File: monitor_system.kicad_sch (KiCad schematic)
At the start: 3 parts, among them K1 DIPxx-1Axx-11x, U1 ACS781xLRTR-050B, U2 L7805

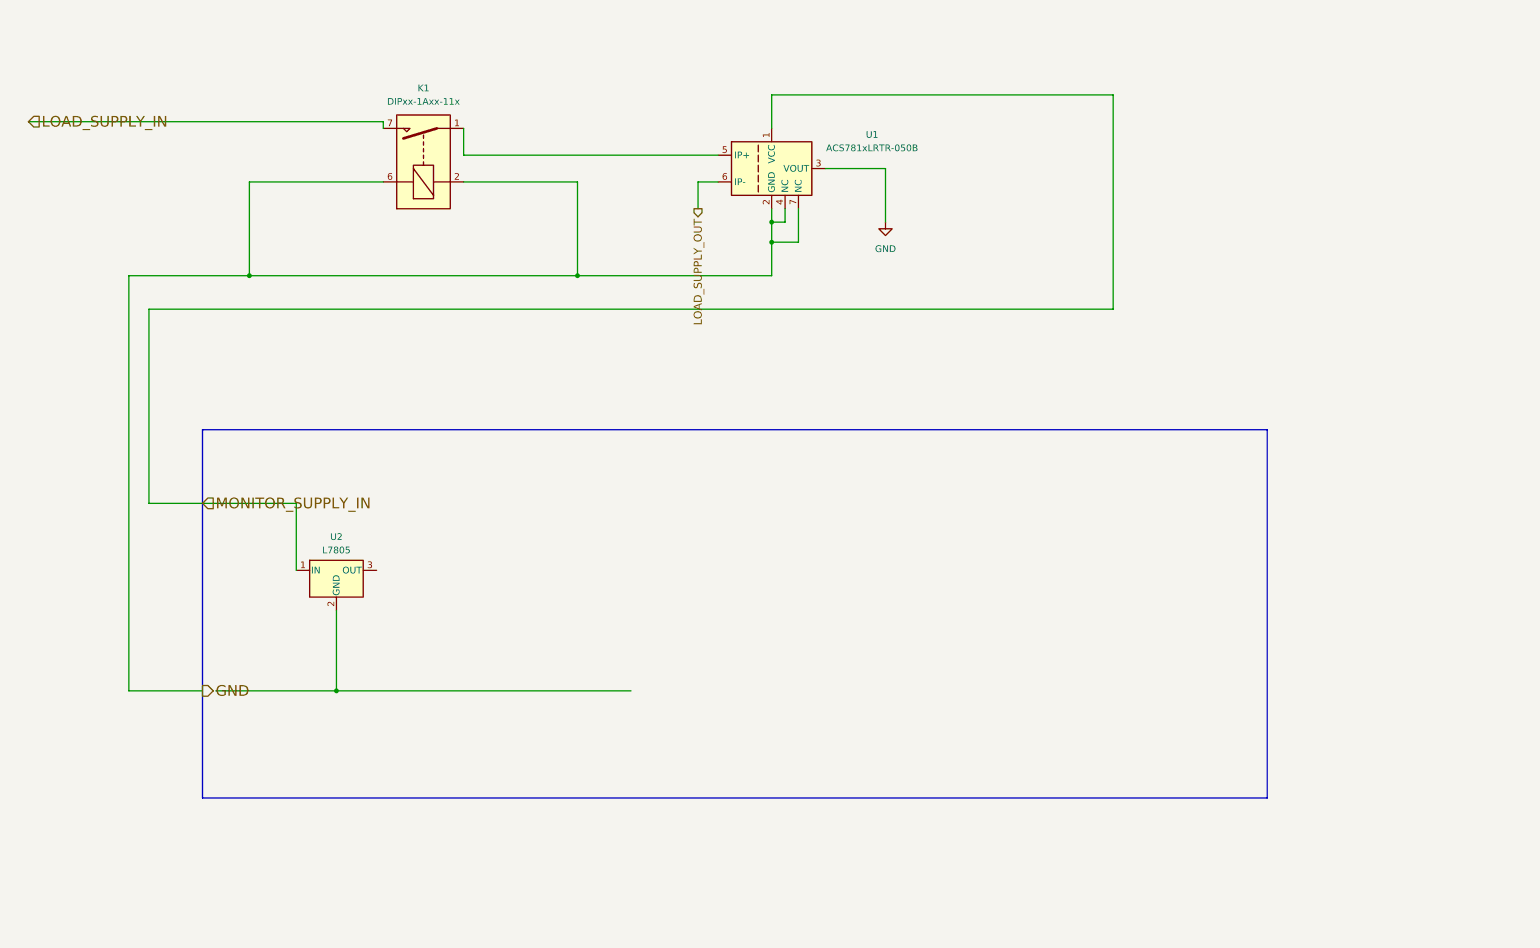
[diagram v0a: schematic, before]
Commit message: feat: new Circuit elements in the schematic and new LTspice Model
feat:added latch in kicad schematic with relative sheet

feat:added Analog-comparator in kicad schematic

feat:added LTspice Analog-comparator model

feat:added spice model into Models folder for the Analog_comparator

refactor:moved all LTspice simulation in a single folder for each one
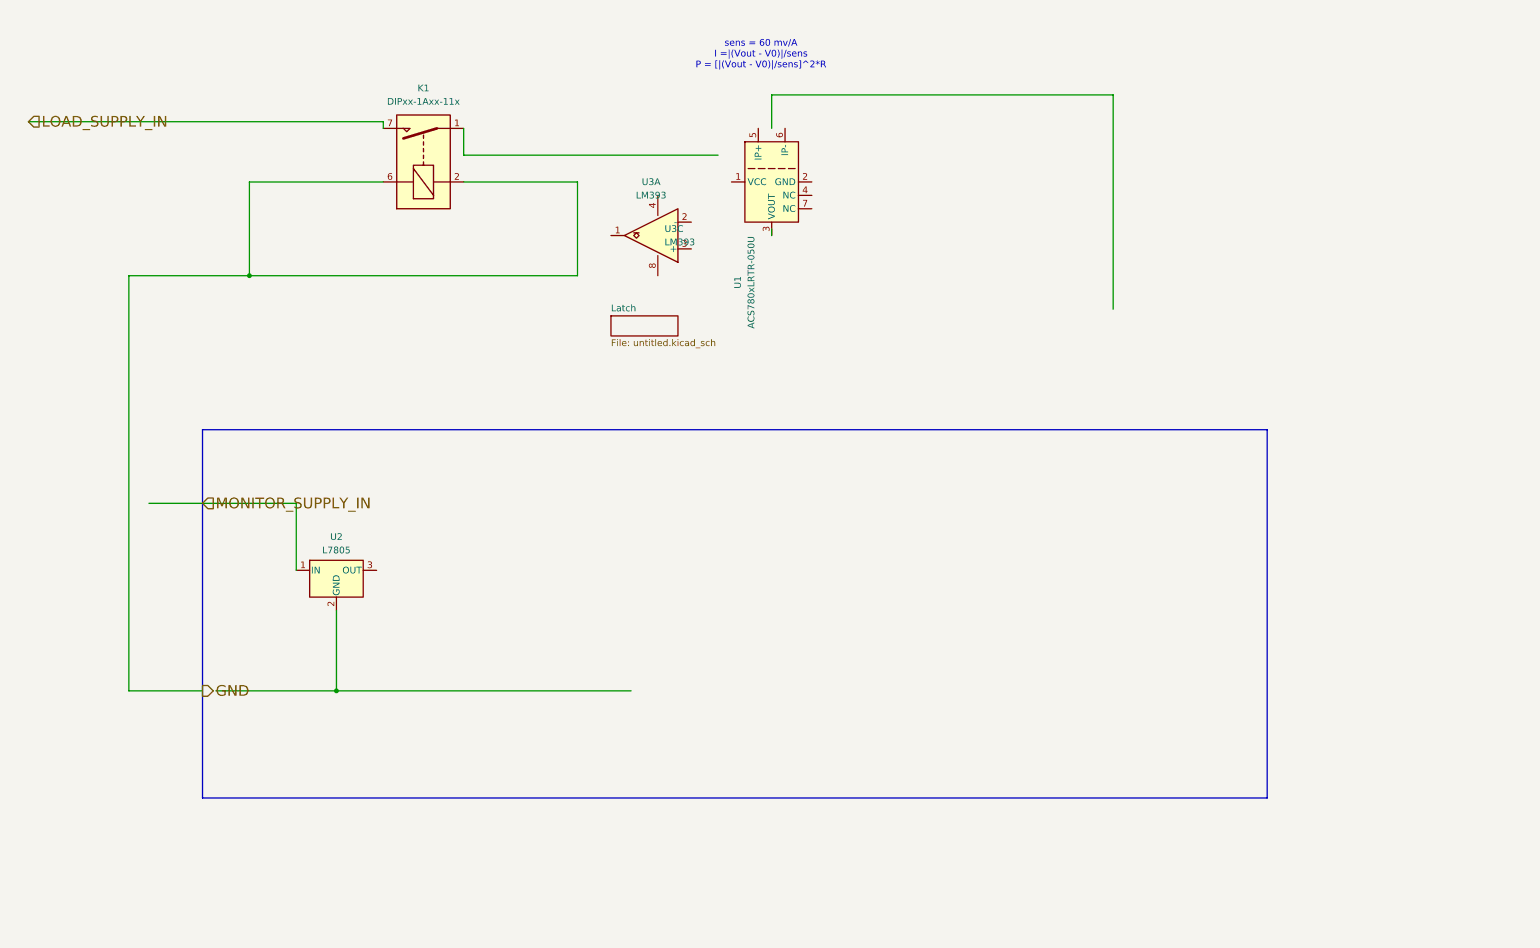
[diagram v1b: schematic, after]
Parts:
- removed U1: ACS781xLRTR-050B, Sensor_Current:Allegro_PSOF-7_4.8x6.4mm_P1.60mm, symbol Sensor_Current:ACS781xLRTR-050B
- added U1: ACS780xLRTR-050U, Sensor_Current:Allegro_PSOF-7_4.8x6.4mm_P1.60mm, symbol Sensor_Current:ACS780xLRTR-050U
- added U3: LM393, symbol Comparator:LM393
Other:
- added sheet Latch (untitled.kicad_sch)
- note added: "sens = 60 mv/A I =|(Vout - V0)|/sens P = [|(Vout - V0)|/sens]^2*R"

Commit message: feat + fix + refactor on the kicad schematic and simulation folder
feat:added transistor for coil supply

refractor: deleted latch sheet

feat: added latch connection

refractor: the monito logic and the supply are now separated

feat:added labels for connection

feat:added falstad NAND latch simulation

ERC = not tested
DRC = not tested
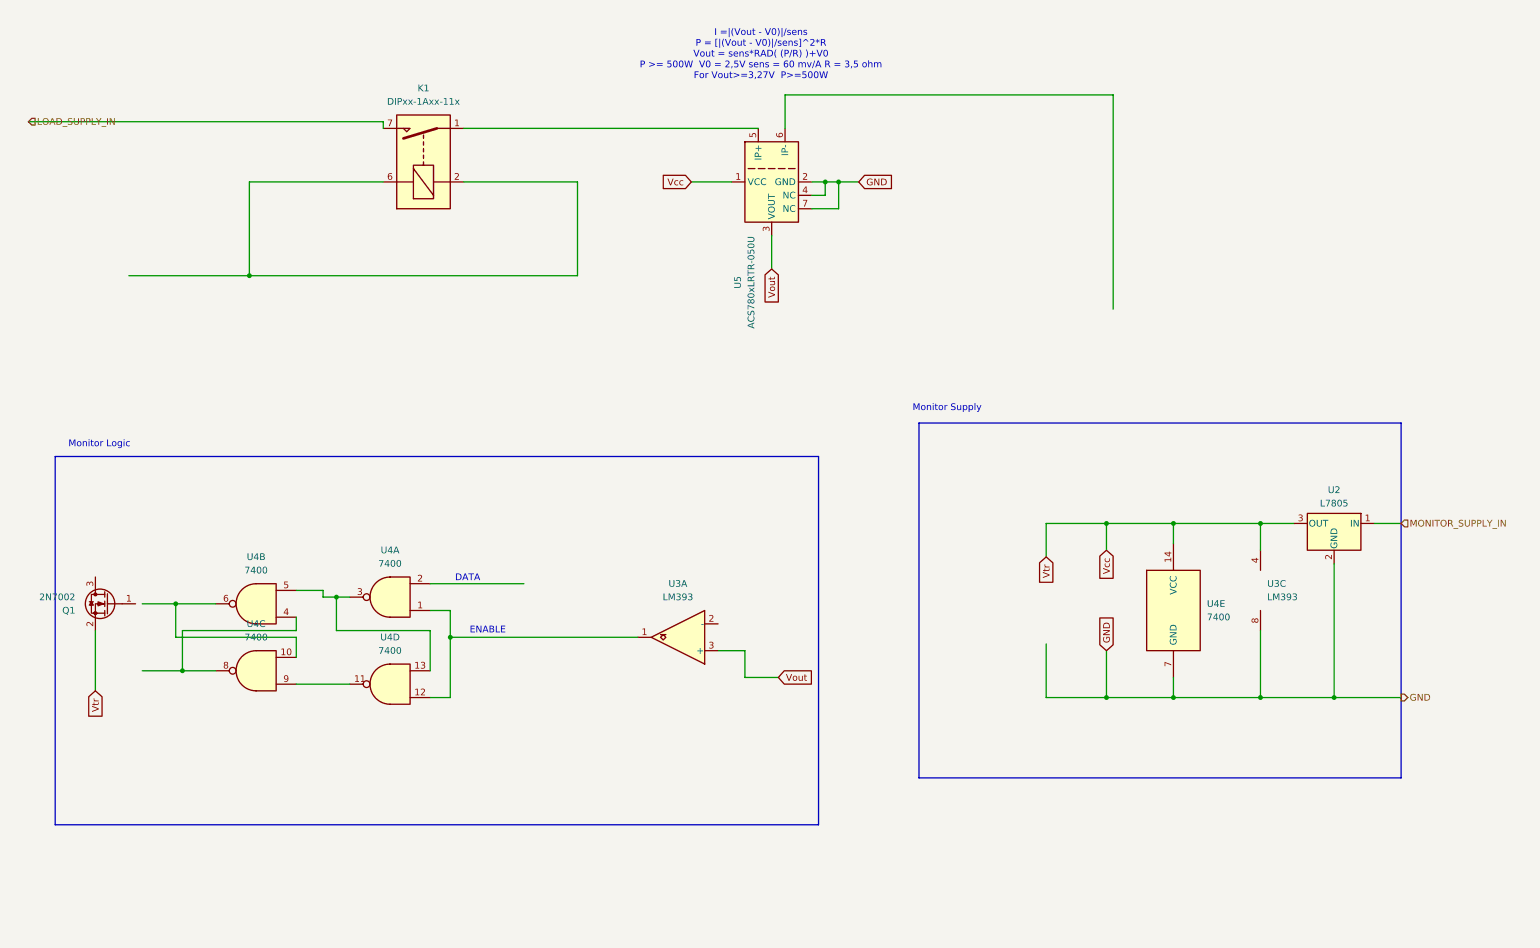
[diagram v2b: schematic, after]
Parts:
- removed U1: ACS780xLRTR-050U, Sensor_Current:Allegro_PSOF-7_4.8x6.4mm_P1.60mm, symbol Sensor_Current:ACS780xLRTR-050U
- added Q1: 2N7002, Package_TO_SOT_SMD:SOT-23, symbol Transistor_FET:2N7002
- added unit 3 of U3
- added U4: 7400, symbol 74xx:7400
- added U5: ACS780xLRTR-050U, Sensor_Current:Allegro_PSOF-7_4.8x6.4mm_P1.60mm, symbol Sensor_Current:ACS780xLRTR-050U
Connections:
- net GND: now also U2.2 (GND), U3.8 (V+), U4.7 (GND), U5.2 (GND), U5.4 (NC), U5.7 (NC); no longer K1.2, K1.6
- net at K1.1, K1.14: now also U5.5 (IP+)
- net at U3.1: now also U4.1, U4.12
- net Vout: now reaches U3.3 (+)
- net Vout: now also U5.3 (VOUT)
- net Vcc: now reaches U2.3 (OUT)
- net Vcc: now also Q1.2 (S), U3.4 (V-), U4.14 (VCC), U5.1 (VCC)
- new net: U4.10, U4.6
- new net: U4.4, U4.8
- new net: U4.11, U4.9
- new net: U4.13, U4.3, U4.5
- new net: K1.2, K1.6
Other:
- removed sheet Latch
- note added: "DATA"
- note added: "ENABLE"
- note added: "I =|(Vout - V0)|/sens P = [|(Vout - V0)|/sens]^2*R Vout = sens*RAD( (P/R) )+V0 P >= 500W V0 = 2,5V sens = 60 mv/A R = 3,5 ohm For Vout>=3,27V P>=500W"
- note added: "Monitor Logic"
- note added: "Monitor Supply"
- note removed: "sens = 60 mv/A I =|(Vout - V0)|/sens P = [|(Vout - V0)|/sens]^2*R"
- moved on the sheet: U2, U3A

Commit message: feat on the kicad schematic and the simulation folder
feat:added voltage Divider

feat:added ED555 ltSpice simulation

feat:added ED555 power cycle timer connection in kicad schematic

ERC:errors(1) warnings(3)
DRC:not tested
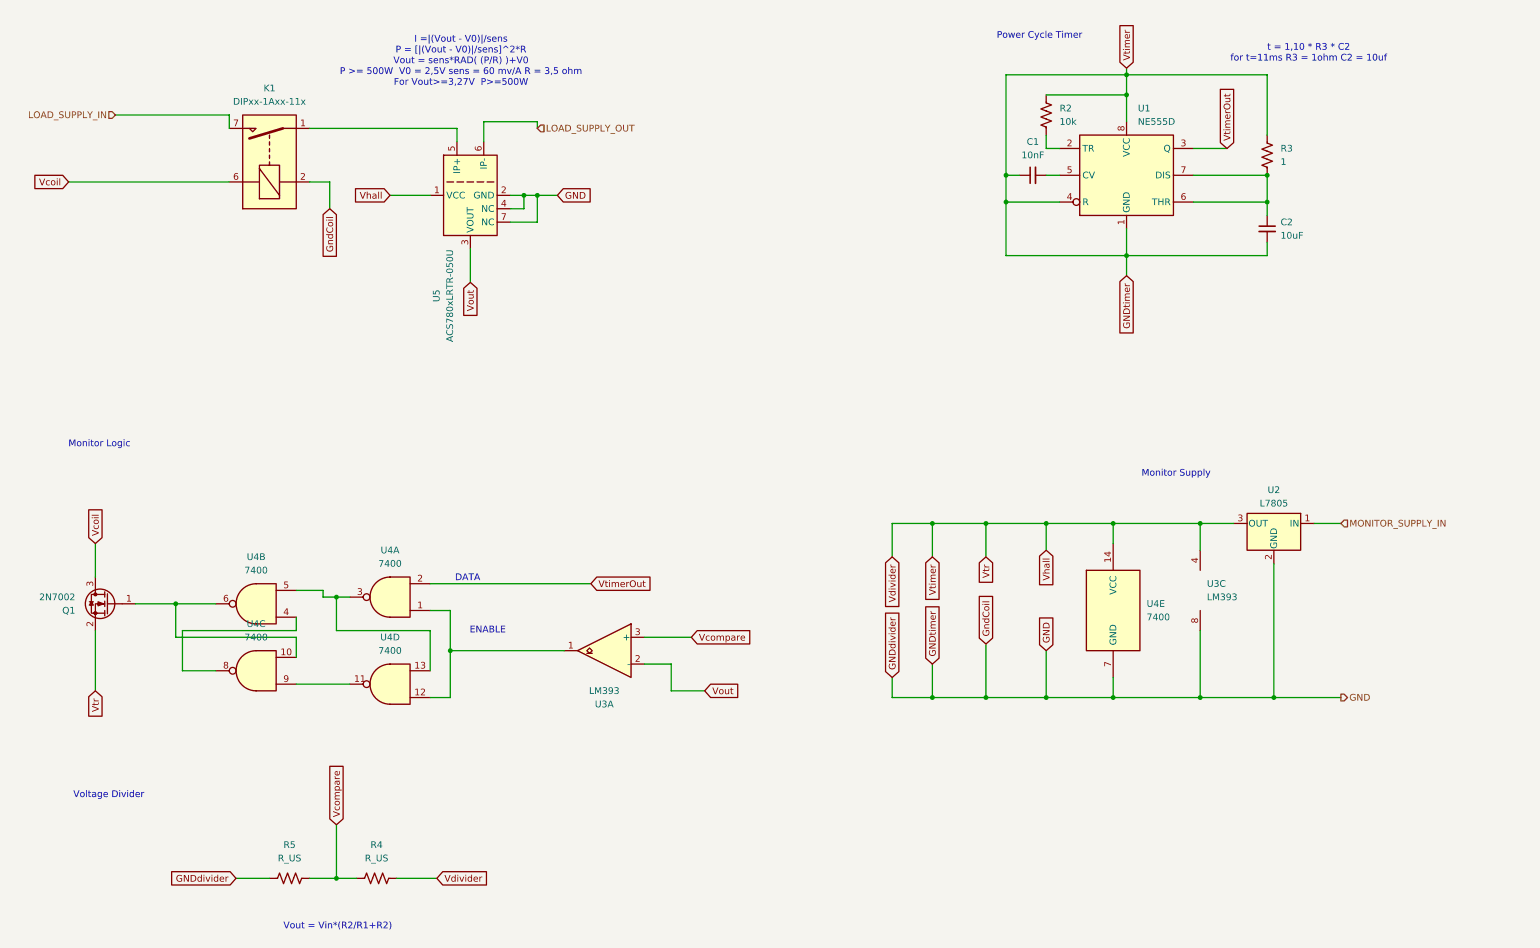
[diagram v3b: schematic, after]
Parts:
- added C1: 10nF, symbol Device:C_Small
- added C2: 10uF, symbol Device:C_Small
- added R2: 10k, symbol Device:R_US
- added R3: 1, symbol Device:R_US
- added R4, R5: R_US, symbol Device:R_US
- added U1: NE555D, Package_SO:SOIC-8_3.9x4.9mm_P1.27mm, symbol Timer:NE555D
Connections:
- net Vcc is gone; now on net GND: Q1.2 (S), U2.3 (OUT), U3.4 (V-), U4.14 (VCC), U5.1 (VCC)
- net GND: now also K1.2, C1.1, C2.2, R2.1, R3.1, R4.2, R5.1, U1.1 (GND), U1.4 (R), U1.8 (VCC)
- net Vout: now also U3.2 (-); no longer U3.3 (+)
- net LOAD_SUPPLY_OUT: now reaches U5.6 (IP-)
- net at U4.10, U4.6: now also Q1.1 (G)
- net Vcoil: now reaches K1.6
- net Vcoil: now also Q1.3 (D); no longer K1.2
- net VtimerOut: now reaches U4.2
- net VtimerOut: now also U1.3 (Q)
- new net: C1.2, U1.5 (CV)
- new net: R2.2, U1.2 (TR)
- new net: C2.1, R3.2, U1.6 (THR), U1.7 (DIS)
- new net Vcompare: R4.1, R5.2, U3.3 (+)
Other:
- note added: "Power Cycle Timer"
- note added: "Voltage Divider"
- note added: "Vout = Vin*(R2/R1+R2)"
- note added: "t = 1,10 * R3 * C2 for t=11ms R3 = 1ohm C2 = 10uf"
- moved on the sheet: K1, U2, U3A, U3C, U4E, U5

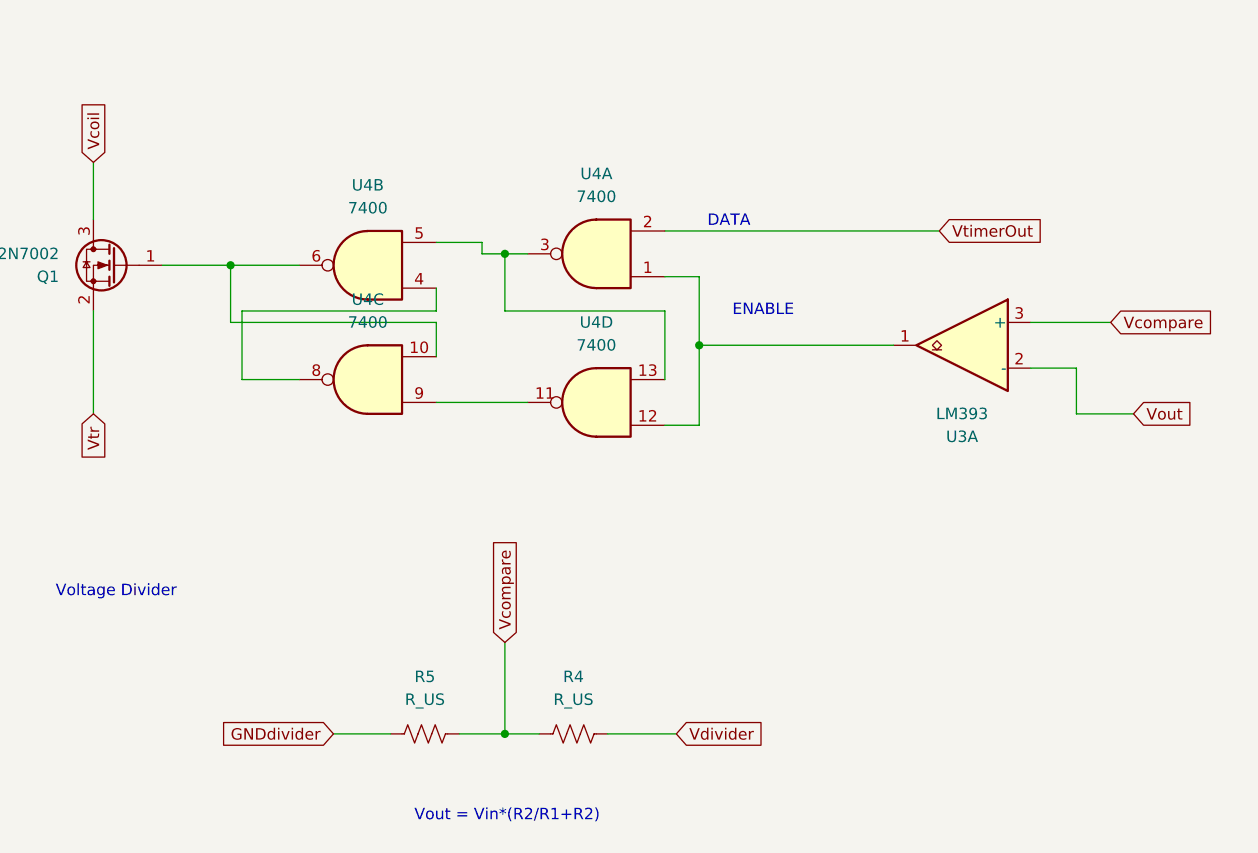
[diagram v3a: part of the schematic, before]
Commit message: feat and fix on kicad schematic and pcb
feat:added resistor capacitor and latch footprints

feat:added elements in pcb design

fix: added pull resistors on analog comparator and NAND latch

ERC: passed warnings(3)
DRC: not tested
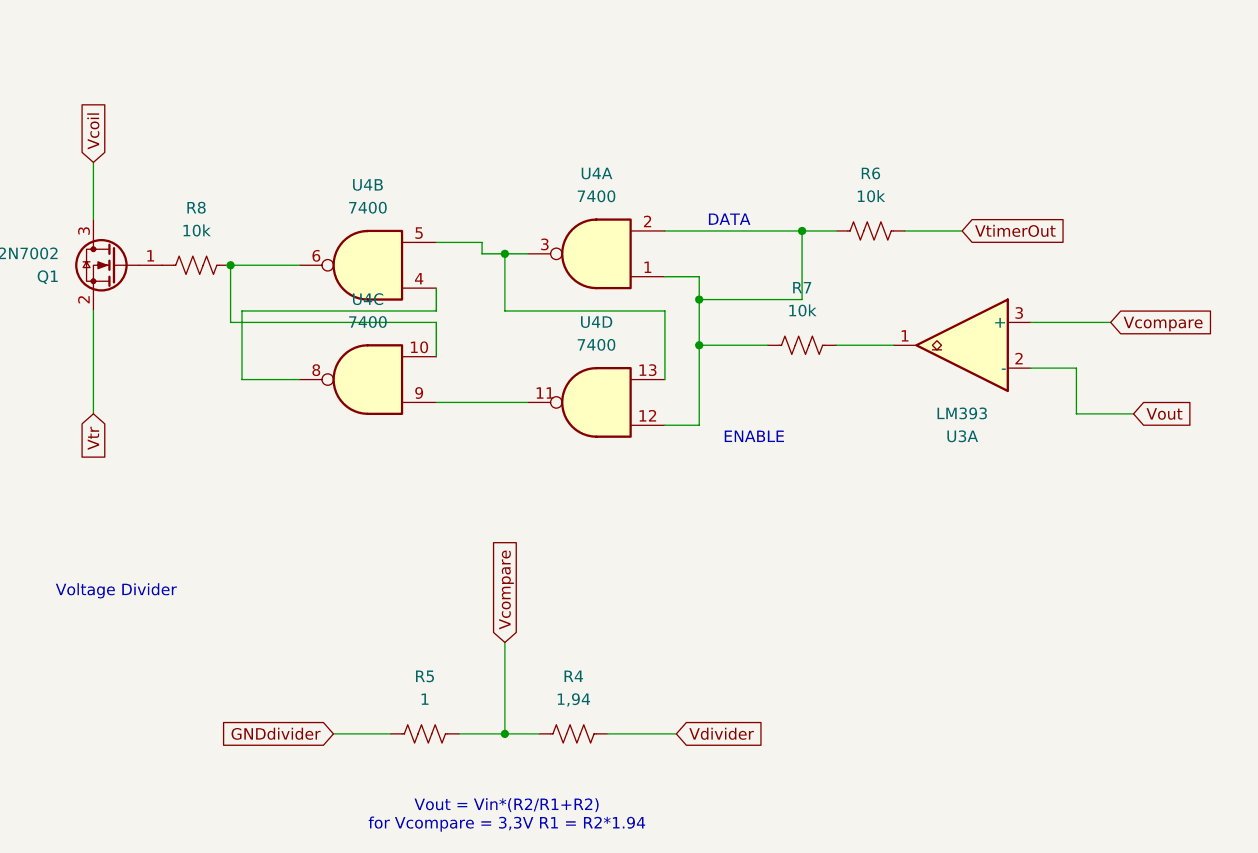
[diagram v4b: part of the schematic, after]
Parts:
- added R6, R7, R8: 10k, symbol Device:R_US
- R4: value R_US -> 1,94
- R5: value R_US -> 1
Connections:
- net VtimerOut: now also R6.2; no longer U4.2
- net at U4.10, U4.6: now also R8.2; no longer Q1.1 (G)
- net at U4.1, U4.12: now also U4.2, R6.1, R7.1; no longer U3.1
- new net: R7.2, U3.1
- new net: Q1.1 (G), R8.1
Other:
- note added: "Vout = Vin*(R2/R1+R2) for Vcompare = 3,3V R1 = R2*1.94"
- note removed: "Vout = Vin*(R2/R1+R2)"

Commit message: feat + fix on kicad pcb
feat:added mass layer

refactor: moved components for better connection

fix:added missing footprints to resistors etc.

ERC: passed warnings(3)
DRC: errors(42) ;(
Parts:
- C1, C2: footprint (none) -> Capacitor_SMD:C_0201_0603Metric
- R2, R3, R4, R5, R6, R7, R8: footprint (none) -> Resistor_SMD:R_0201_0603Metric
- U2: footprint (none) -> Package_TO_SOT_SMD:TO-252-2
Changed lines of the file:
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@@
 			)
 		)
-		(property "Footprint" ""
+		(property "Footprint" "Capacitor_SMD:C_0201_0603Metric"
 			(at 204.47 44.45 0)
 			(effects
@@
 			)
 		)
-		(property "Footprint" ""
+		(property "Footprint" "Resistor_SMD:R_0201_0603Metric"
 			(at 80.264 176.784 90)
 			(effects
@@
 			)
 		)
-		(property "Footprint" ""
+		(property "Footprint" "Resistor_SMD:R_0201_0603Metric"
 			(at 208.026 33.274 90)
 			(effects
@@
 			)
 		)
-		(property "Footprint" ""
+		(property "Footprint" "Resistor_SMD:R_0201_0603Metric"
 			(at 113.284 120.904 90)
 			(effects
@@
 			)
 		)
-		(property "Footprint" ""
+		(property "Footprint" "Capacitor_SMD:C_0201_0603Metric"
 			(at 248.92 54.61 0)
 			(effects
@@
 			)
 		)
-		(property "Footprint" ""
+		(property "Footprint" "Resistor_SMD:R_0201_0603Metric"
 			(at 38.354 124.714 90)
 			(effects
@@
 			)
 		)
-		(property "Footprint" ""
+		(property "Footprint" "Resistor_SMD:R_0201_0603Metric"
 			(at 63.754 176.784 90)
 			(effects
@@
 			)
 		)
-		(property "Footprint" ""
+		(property "Footprint" "Resistor_SMD:R_0201_0603Metric"
 			(at 249.936 40.894 90)
 			(effects
@@
 			)
 		)
-		(property "Footprint" ""
+		(property "Footprint" "Package_TO_SOT_SMD:TO-252-2"
 			(at 249.555 114.3 0)
 			(effects
@@
 			)
 		)
-		(property "Footprint" ""
+		(property "Footprint" "Resistor_SMD:R_0201_0603Metric"
 			(at 105.664 133.604 90)
 			(effects
